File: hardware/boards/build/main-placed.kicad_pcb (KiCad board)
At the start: 4 copper layers, 103 x 84 mm, 146 parts

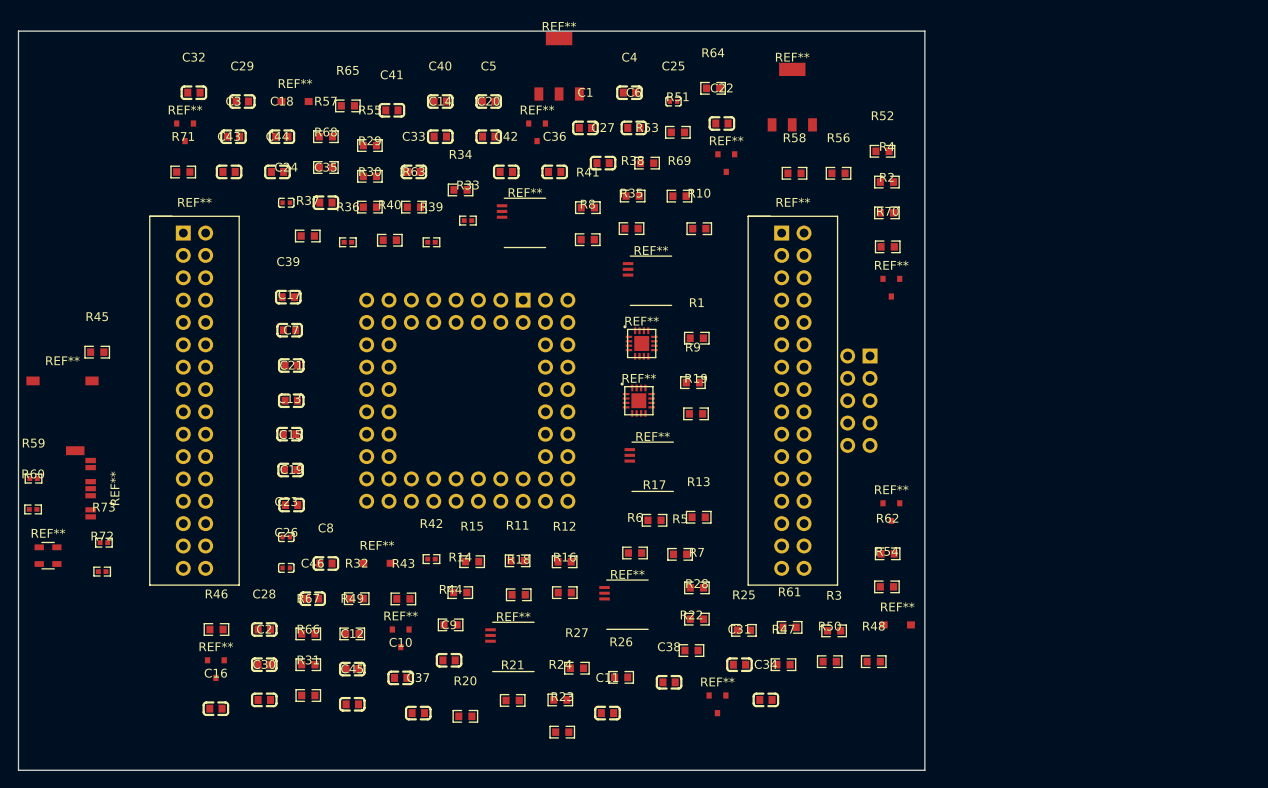
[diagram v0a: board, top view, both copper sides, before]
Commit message: Update parts and placement algos
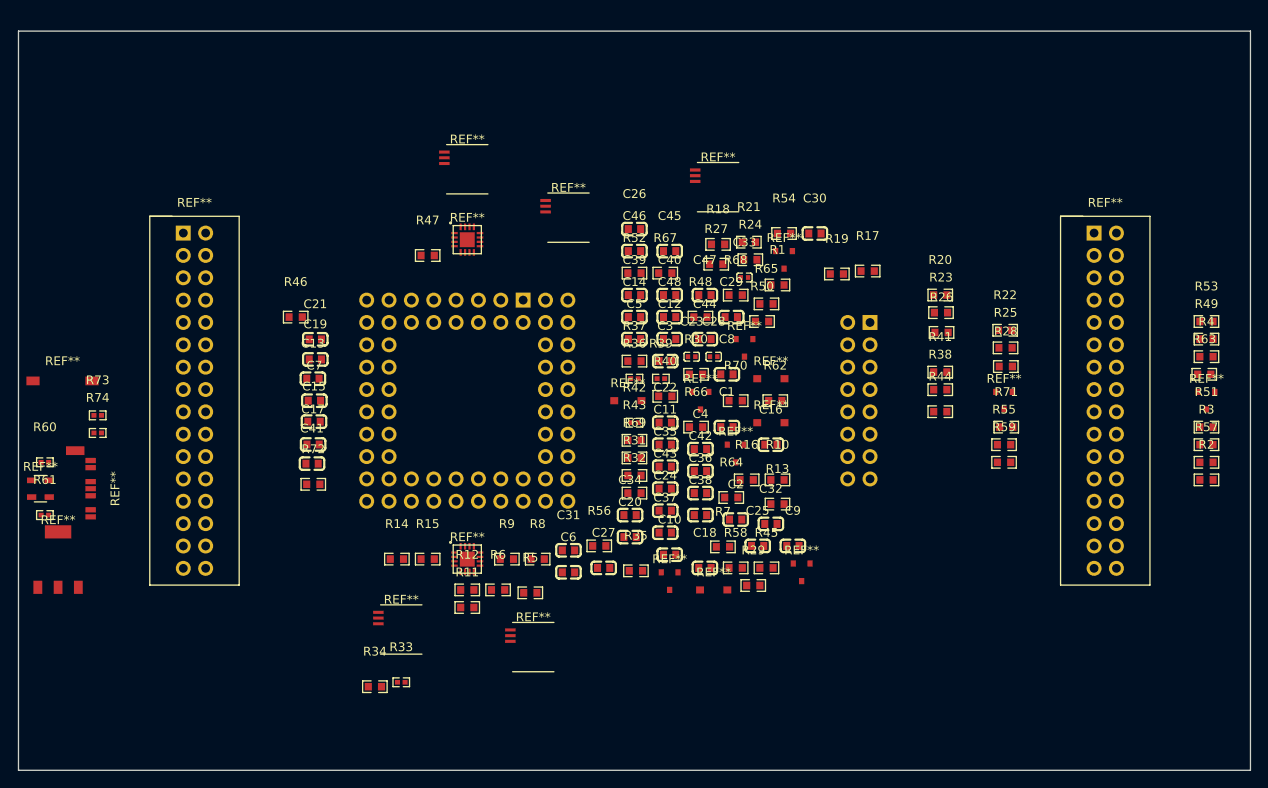
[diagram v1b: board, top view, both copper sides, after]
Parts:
- removed the REF** at (70.5, 42.0)
- removed the REF** at (61.4, 4.00)
- removed the REF** at (69.2, 65.2)
- removed the REF** at (31.4, 8.00)
- removed the REF** at (70.8, 35.5)
- removed the REF** at (99.9, 67.5)
- removed the REF** at (99.2, 54.7)
- removed the REF** at (57.6, 21.8)
- removed the REF** at (18.9, 11.5)
- removed the REF** at (58.9, 11.5)
- removed the REF** at (80.4, 15.0)
- removed the REF** at (43.4, 69.0)
- removed the REF** at (72.1, 49.5)
- removed the REF** at (95.5, 42.0)
- removed the REF** at (71.9, 28.4)
- removed the REF** at (56.2, 70.0)
- removed the REF** at (22.4, 72.5)
- removed the REF** at (40.7, 60.5)
- removed the REF** at (99.2, 29.2)
- removed the REF** at (79.4, 76.5)
- added C47: 100nF, YAGEO_CC0603KRX7R9BB104:C0603, F.Cu at (78.0, 30.0)
- added C48: 10nF, FH_0603B103K500NT:C0603, F.Cu at (74.0, 32.5)
- added R74: 27Ω, UNI_ROYAL_0402WGF270JTCE:R0402, F.Cu at (9.00, 45.7)
- added REF**: TSSOP-14, OPA4171AIPWR:TSSOP-14, F.Cu at (43.5, 68.0)
- added REF**: WQFN-16, DAC80508ZRTER:WQFN-16, F.Cu at (51.0, 60.0)
- added REF**: TSSOP-14, OPA4171AIPWR:TSSOP-14, F.Cu at (62.5, 21.2)
- added REF**: SOT-23, BAT54S:SOT-23, F.Cu at (77.5, 42.0)
- added REF**: SOD-123, B5819W:SOD-123, F.Cu at (79.0, 63.5)
- added REF**: SOT-23, BAT54S:SOT-23, F.Cu at (81.5, 48.0)
- added REF**: SOT-23, 2N3904:SOT-23, F.Cu at (112.0, 42.0)
- added REF**: SOT-23, BAT54S:SOT-23, F.Cu at (87.0, 26.0)
- added REF**: SOD-123, B5819W:SOD-123, F.Cu at (85.5, 39.5)
- added REF**: SOD-123, B5819W:SOD-123, F.Cu at (69.2, 42.0)
- added REF**: SOT-23, BAT54S:SOT-23, F.Cu at (74.0, 62.5)
- added REF**: TSSOP-14, OPA4171AIPWR:TSSOP-14, F.Cu at (51.0, 15.7)
- added REF**: SOT-23, 2N3904:SOT-23, F.Cu at (135.0, 42.0)
- added REF**: Eurorack_2x8, EurorackPowerHeader16:EurorackPowerHeader_2x8, B.Cu at (95.5, 42.0)
- added REF**: WQFN-16, DAC80508ZRTER:WQFN-16, F.Cu at (51.0, 23.7)
- added REF**: TSSOP-14, OPA4171AIPWR:TSSOP-14, F.Cu at (58.5, 70.0)
- added REF**: SOT-23, BAT54S:SOT-23, F.Cu at (89.0, 61.5)
- added REF**: TSSOP-14, OPA4171AIPWR:TSSOP-14, F.Cu at (79.5, 17.7)
- added REF**: SOD-123, B5819W:SOD-123, F.Cu at (85.5, 44.5)
- added REF**: SOT-23, BAT54S:SOT-23, F.Cu at (82.5, 36.0)
- C24, C26: value 1µF -> 100nF; footprint Samsung_Electro_Mechanics_CL05A105KA5NQNC:C0402 -> YAGEO_CC0603KRX7R9BB104:C0603
- C25: value 1µF -> 10µF; footprint Samsung_Electro_Mechanics_CL05A105KA5NQNC:C0402 -> Samsung_Electro_Mechanics_CL10A106KP8NNNC:C0603
- C27, C31, C36, C41, C42: value 100nF -> 10µF; footprint YAGEO_CC0603KRX7R9BB104:C0603 -> Samsung_Electro_Mechanics_CL10A106KP8NNNC:C0603
- C28: value 100nF -> 1µF; footprint YAGEO_CC0603KRX7R9BB104:C0603 -> Samsung_Electro_Mechanics_CL05A105KA5NQNC:C0402
- C29, C32, C40: value 10µF -> 100nF; footprint Samsung_Electro_Mechanics_CL10A106KP8NNNC:C0603 -> YAGEO_CC0603KRX7R9BB104:C0603
- C33: value 100nF -> 2.2µF; footprint YAGEO_CC0603KRX7R9BB104:C0603 -> Samsung_Electro_Mechanics_CL05A225MQ5NSNC:C0402
- C43: value 100nF -> 10nF; footprint YAGEO_CC0603KRX7R9BB104:C0603 -> FH_0603B103K500NT:C0603
- R45: value 10kΩ -> 200Ω; footprint UNI_ROYAL_0603WAF1002T5E:R0603 -> UNI_ROYAL_0603WAF2000T5E:R0603
- R48, R50, R52, R54, R56, R58: value 22kΩ -> 10kΩ; footprint UNI_ROYAL_0603WAF2202T5E:R0603 -> UNI_ROYAL_0603WAF1002T5E:R0603
- R49, R51, R53, R55, R57: value 10kΩ -> 22kΩ; footprint UNI_ROYAL_0603WAF1002T5E:R0603 -> UNI_ROYAL_0603WAF2202T5E:R0603
- R59: value 5.1kΩ -> 22kΩ; footprint UNI_ROYAL_0402WGF5101TCE:R0402 -> UNI_ROYAL_0603WAF2202T5E:R0603
- R61: value 1kΩ -> 5.1kΩ; footprint UNI_ROYAL_0603WAF1001T5E:R0603 -> UNI_ROYAL_0402WGF5101TCE:R0402
- R63, R71: value 10kΩ -> 1kΩ; footprint UNI_ROYAL_0603WAF1002T5E:R0603 -> UNI_ROYAL_0603WAF1001T5E:R0603
- R69: value 1kΩ -> 10kΩ; footprint UNI_ROYAL_0603WAF1001T5E:R0603 -> UNI_ROYAL_0603WAF1002T5E:R0603
- R72: value 27Ω -> 10kΩ; footprint UNI_ROYAL_0402WGF270JTCE:R0402 -> UNI_ROYAL_0603WAF1002T5E:R0603
- moved R59 110.3 mm to (112.0, 49.0)
- moved R57 106.7 mm to (135.0, 49.0)
- moved R49 102.7 mm to (135.0, 35.0)
- moved REF** 98.6 mm to (4.50, 60.1)
- moved R71 97.9 mm to (112.2, 45.0)
- moved R63 91.8 mm to (134.8, 39.0)
- moved R61 85.6 mm to (3.00, 55.0)
- moved C30 82.0 mm to (90.5, 23.0)
- moved C32 81.9 mm to (85.5, 56.0)
- moved R45 79.9 mm to (85.0, 61.0)
- moved R55 79.7 mm to (112.0, 47.0)
- moved R20 72.1 mm to (104.8, 30.0)
- moved C16 69.8 mm to (85.5, 47.0)
- moved R51 68.8 mm to (135.0, 45.0)
- moved C18 68.6 mm to (78.0, 61.0)
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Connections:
- C24 pad 1: c_ref1-power-hv -> c_ref1_hf-power-hv
- C25 pad 1: c_ref2-power-hv -> c_ref1_hf-power-hv
- C26 pad 1: c_ref_filt-power-hv -> c_ref2_hf-power-hv
- C27 pad 1: c_vio2-power-hv -> c_ref2_hf-power-hv
- C28 pad 1: c_vio2-power-hv -> c_ref_filt-power-hv
- C29 pad 1: c_3v3_bulk-power-hv -> c_vio2-power-hv
- C30 pad 1: c_3v3_bulk-power-hv -> c_vio2-power-hv
- C31 pad 1: c_aref-power-hv -> c_3v3_bulk-power-hv
- C32 pad 1: c_vb-power-hv -> c_3v3_bulk-power-hv
- C33 pad 1: c_dac2_2-power-hv -> c_aref-power-hv
- C34 pad 1: c_vio2-power-hv -> c_vb_hf-power-hv
- C35 pad 1: c_vio2-power-hv -> c_vb_hf-power-hv
- C36 pad 1: c_op5_p-power-hv -> c_dac2_2-power-hv
- C37 pad 1: c_dac2_2-power-hv -> c_vio2-power-hv
- C38 pad 1: c_dac2_2-power-hv -> c_vio2-power-hv
- C39 pad 1: hv -> c_dac2_2-power-hv
- C39 pad 2: lv -> hv
- C40 pad 1: c_op5_p-power-hv -> c_dac2_2-power-hv
- C41 pad 1: c_filter-power-hv -> hv
- C41 pad 2: hv -> lv
- C42 pad 1: c_filter-power-hv-1 -> c_op5_p-power-hv
- C43 pad 1: c_filter-power-hv-2 -> c_filter-power-hv
- C44 pad 1: c_filter-power-hv-3 -> c_filter-power-hv-1
- C45 pad 1: c_filter-power-hv-4 -> c_filter-power-hv-2
- C46 pad 1: c_filter-power-hv-5 -> c_filter-power-hv-3
- R17 pad 1: 1 -> pitch1
- R20 pad 1: dac-7 -> pitch2
- R23 pad 1: dac-8 -> pitch3
- R26 pad 1: 14 -> pitch4
- R45 pad 2: BS -> c_aref-power-hv
- R46 pad 2: RUN -> BS
- R47 pad 1: c_filter-power-hv -> c_3v3_bulk-power-hv
- R47 pad 2: hv -> RUN
- R48 pad 1: clk_in -> c_filter-power-hv
- R48 pad 2: c_filter-power-hv -> hv
- R49 pad 1: c_filter-power-hv-1 -> clk_in
- R49 pad 2: hv -> c_filter-power-hv
- R50 pad 1: cv_a -> c_filter-power-hv-1
- R50 pad 2: c_filter-power-hv-1 -> hv
- R51 pad 1: c_filter-power-hv-2 -> cv_a
- R51 pad 2: hv -> c_filter-power-hv-1
- R52 pad 1: cv_b -> c_filter-power-hv-2
- R52 pad 2: c_filter-power-hv-2 -> hv
- R53 pad 1: c_filter-power-hv-3 -> cv_b
- R53 pad 2: hv -> c_filter-power-hv-2
- R54 pad 1: cv_c -> c_filter-power-hv-3
- R54 pad 2: c_filter-power-hv-3 -> hv
- R55 pad 1: c_filter-power-hv-4 -> cv_c
- R55 pad 2: hv -> c_filter-power-hv-3
- R56 pad 1: cv_d -> c_filter-power-hv-4
- R56 pad 2: c_filter-power-hv-4 -> hv
- R57 pad 1: c_filter-power-hv-5 -> cv_d
- R57 pad 2: hv -> c_filter-power-hv-4
- R58 pad 1: input -> c_filter-power-hv-5
- R58 pad 2: c_filter-power-hv-5 -> hv
- R59 pad 1: 5-1 -> input
- R59 pad 2: hv -> c_filter-power-hv-5
- R60 pad 1: 6-1 -> 5-1
- R61 pad 1: clk_out -> 6-1
- R61 pad 2: BASE -> hv
- R62 pad 1: c_dac2_2-power-hv -> clk_out
- R62 pad 2: COLLECTOR -> BASE
- R63 pad 1: c_vio2-power-hv -> c_dac2_2-power-hv
- R63 pad 2: c_enc_a_a-power-hv -> COLLECTOR
- R64 pad 2: c_enc_a_b-power-hv -> c_enc_a_a-power-hv
- R65 pad 2: c_enc_a_sw-power-hv -> c_enc_a_b-power-hv
- R66 pad 2: c_enc_b_a-power-hv -> c_enc_a_sw-power-hv
- R67 pad 2: c_enc_b_b-power-hv -> c_enc_b_a-power-hv
- R68 pad 2: c_enc_b_sw-power-hv -> c_enc_b_b-power-hv
- R69 pad 1: rst_out -> c_vio2-power-hv
- R69 pad 2: BASE-1 -> c_enc_b_sw-power-hv
- R70 pad 1: c_dac2_2-power-hv -> rst_out
- R70 pad 2: COLLECTOR-1 -> BASE-1
- R71 pad 1: c_vio2-power-hv -> c_dac2_2-power-hv
- R71 pad 2: sd_cd -> COLLECTOR-1
- R72 pad 1: usb_dm -> c_vio2-power-hv
- R72 pad 2: DM -> sd_cd
- R73 pad 1: usb_dp -> usb_dm
- R73 pad 2: 3 -> DM
- REF** pad 19: 19 -> c_enc_b_a-power-hv
- REF** pad 20: 20 -> c_enc_b_b-power-hv
- REF** pad 21: 21 -> c_enc_b_sw-power-hv
- REF** pad 1: hv -> VBUS
- REF** pad 10: cv_a -> cv_c
- REF** pad 11: cv_b -> cv_d
- REF** pad 12: cv_c -> hv
- REF** pad 13: cv_d -> gate1
- REF** pad 14: gate1 -> gate2
- REF** pad 15: gate2 -> gate3
- REF** pad 16: gate3 -> gate4
- REF** pad 17: gate4 -> hv
- REF** pad 22: vel1 -> hv
- REF** pad 23: vel2 -> vel1
- REF** pad 24: vel3 -> vel2
- REF** pad 25: vel4 -> vel3
- REF** pad 26: mod1 -> vel4
- REF** pad 27: mod2 -> hv
- REF** pad 28: mod3 -> mod1
- REF** pad 29: mod4 -> mod2
- REF** pad 3: c_enc_b_a-power-hv -> clk_in
- REF** pad 30: c_dac2_2-power-hv -> mod3
- REF** pad 31: hv -> mod4
- REF** pad 4: c_enc_b_b-power-hv -> COLLECTOR
- REF** pad 5: c_enc_b_sw-power-hv -> input
- REF** pad 6: clk_in -> COLLECTOR-1
- REF** pad 7: input -> hv
- REF** pad 8: COLLECTOR -> cv_a
- REF** pad 9: COLLECTOR-1 -> cv_b
- REF** pad 1: c_vb-power-hv -> c_vb_hf-power-hv
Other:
- board size 103 x 84 mm -> 140 x 84 mm
